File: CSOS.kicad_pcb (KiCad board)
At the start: 2 copper layers, 22 parts, among them P101 CONN_01X02, P102 CONN_01X03, P103 CONN_01X02, Q201 BUK9575, U201 LMV358, U401 LM2931D-R

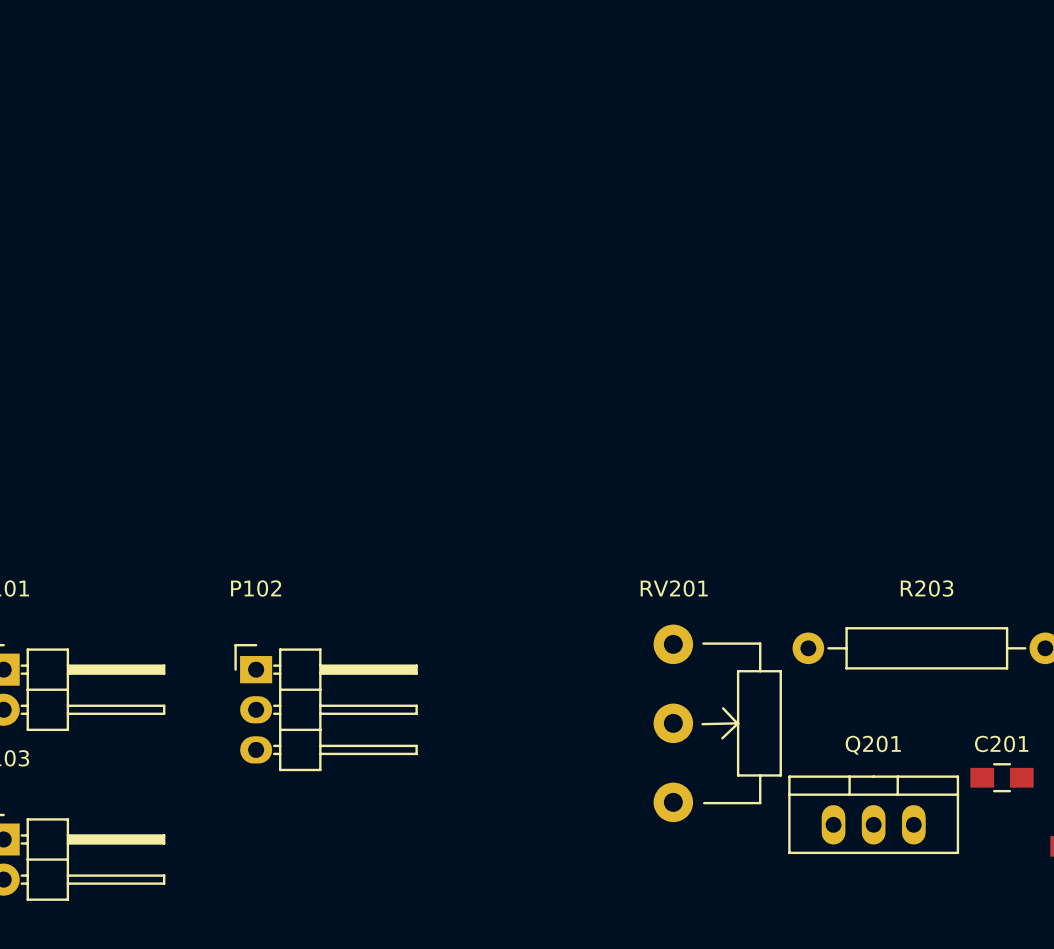
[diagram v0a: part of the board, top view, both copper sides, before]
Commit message: Creating heatsink footprint and adding to schematic and layout.
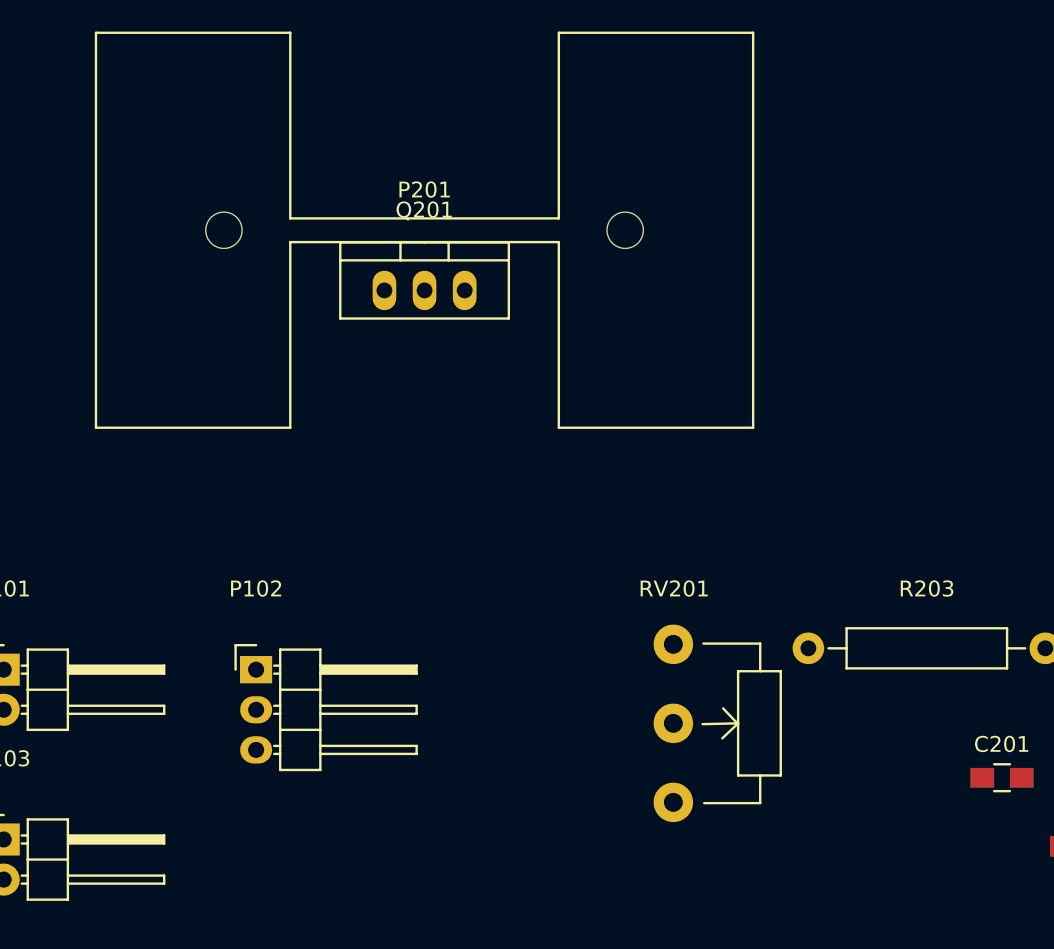
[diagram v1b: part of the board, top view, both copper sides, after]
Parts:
- added P201: CONN_01X01, CSOS:FA-T220-38E, F.Cu at (190.5, 85.1)
- moved Q201 44.2 mm to (190.5, 88.9)
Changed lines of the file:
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@@
     (tracks 0)
     (zones 0)
-    (modules 22)
+    (modules 23)
     (nets 17)
   )
@@
   )
   (module TO_SOT_Packages_THT:TO-220_Neutral123_Vertical (layer F.Cu)
-    (at 218.929001 122.725)
+    (at 190.5 88.9)
     (descr "TO-220, Neutral, Vertical,")
     (tags "TO-220, Neutral, Vertical,")
@@
     )
   )
+  (module CSOS:FA-T220-38E (layer F.Cu)
+    (at 190.5 85.09)
+    (fp_text reference P201 (at 0 -2.54) (layer F.SilkS)
+      (effects (font (size 1 1) (thickness 0.15)))
+    )
+    (fp_text value CONN_01X01 (at 0 -4.445) (layer F.Fab)
+      (effects (font (size 1 1) (thickness 0.15)))
+    )
+    (fp_line (start -20.8 -12.5) (end -8.5 -12.5) (layer F.SilkS) (width 0.15))
+    (fp_line (start 8.5 -12.5) (end 20.8 -12.5) (layer F.SilkS) (width 0.15))
+    (fp_line (start 8.5 12.5) (end 20.8 12.5) (layer F.SilkS) (width 0.15))
+    (fp_line (start -20.8 12.5) (end -8.5 12.5) (layer F.SilkS) (width 0.15))
+    (fp_line (start 8.5 -0.75) (end 8.5 -12.5) (layer F.SilkS) (width 0.15))
+    (fp_line (start -8.5 -0.75) (end -8.5 -12.5) (layer F.SilkS) (width 0.15))
+    (fp_line (start 8.5 0.75) (end 8.5 12.5) (layer F.SilkS) (width 0.15))
+    (fp_line (start -8.5 0.75) (end -8.5 12.5) (layer F.SilkS) (width 0.15))
+    (fp_line (start -8.5 0.75) (end 8.5 0.75) (layer F.SilkS) (width 0.15))
+    (fp_line (start -8.5 -0.75) (end 8.5 -0.75) (layer F.SilkS) (width 0.15))
+    (fp_line (start -20.8 -12.5) (end -20.8 12.5) (layer F.SilkS) (width 0.15))
+    (fp_line (start 20.8 -12.5) (end 20.8 12.5) (layer F.SilkS) (width 0.15))
+    (pad "" np_thru_hole circle (at -12.7 0) (size 2.3 2.3) (drill 2.3) (layers *.Cu *.Mask F.SilkS))
+    (pad "" np_thru_hole circle (at 12.7 0) (size 2.3 2.3) (drill 2.3) (layers *.Cu *.Mask F.SilkS))
+  )
 )

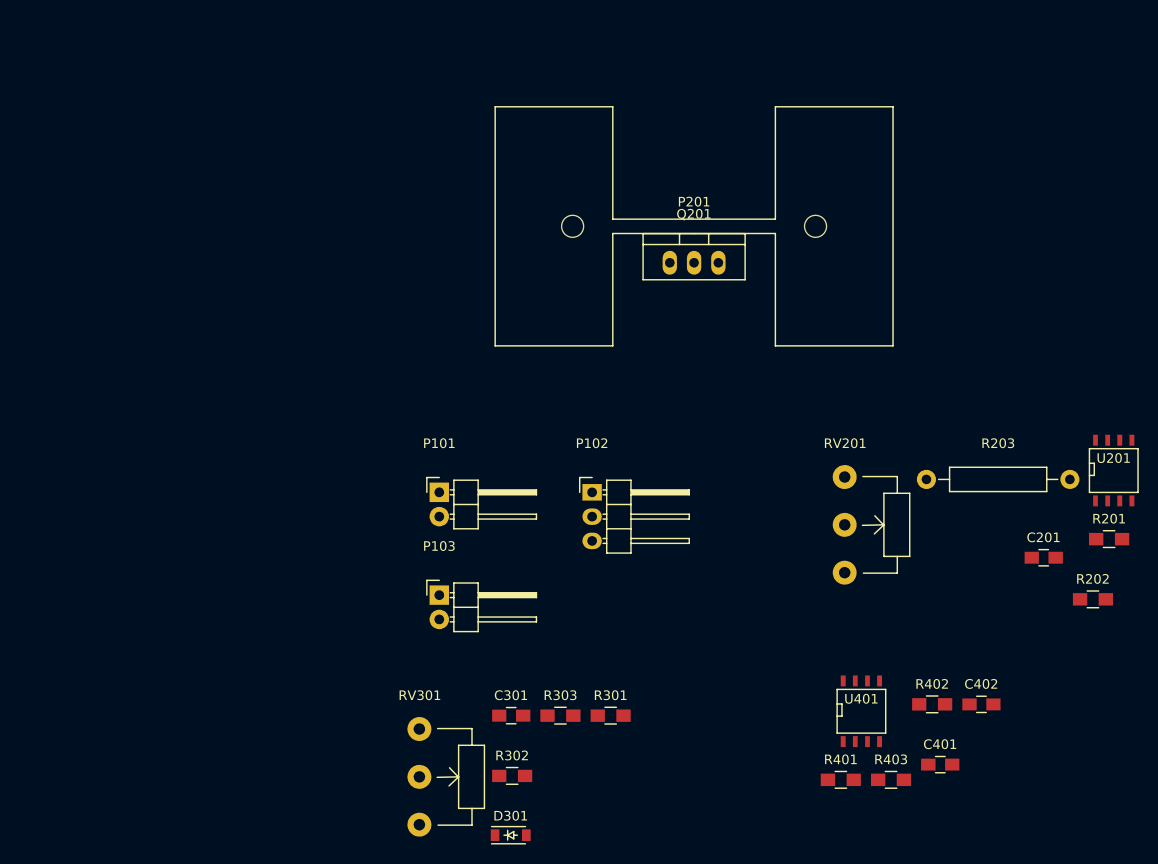
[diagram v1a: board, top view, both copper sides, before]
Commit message: Built 200 mil pitch terminal block. Updated pcb layout with new footprints.
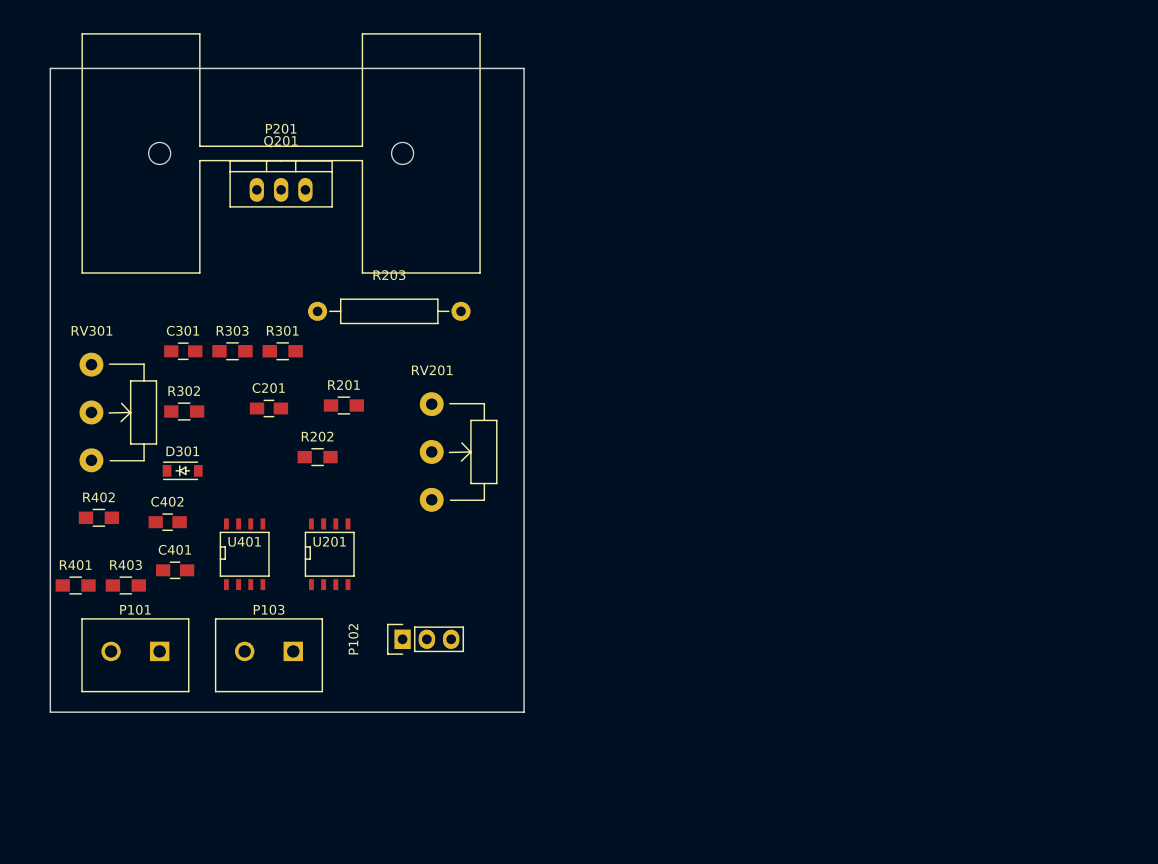
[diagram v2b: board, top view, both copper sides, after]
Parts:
- P101, P103: footprint Pin_Headers:Pin_Header_Angled_1x02 -> CSOS:Terminal_Block_200_mil
- P102: footprint Pin_Headers:Pin_Header_Angled_1x03 -> Pin_Headers:Pin_Header_Straight_1x03
- moved R402 89.3 mm to (128.3, 115.6)
- moved C402 87.2 mm to (135.5, 116.0)
- moved C401 82.5 mm to (136.2, 121.1)
- moved R401 82.5 mm to (125.8, 122.6)
- moved R403 82.5 mm to (131.1, 122.6)
- moved C201 82.5 mm to (146.1, 104.1)
- moved U201 82.4 mm to (152.4, 119.4)
- moved R202 82.4 mm to (151.1, 109.2)
- moved R201 81.2 mm to (153.9, 103.8)
- moved U401 66.5 mm to (143.5, 119.4)
- moved R203 66.0 mm to (151.1, 94.0)
- moved R302 51.3 mm to (137.2, 104.5)
- moved RV301 51.3 mm to (127.5, 99.6)
- moved C301 51.3 mm to (137.1, 98.2)
- moved D301 51.3 mm to (137.0, 110.7)
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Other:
- board outline added: 49.5 x 67.3 mm
